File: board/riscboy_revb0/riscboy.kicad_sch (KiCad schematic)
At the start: 110 parts

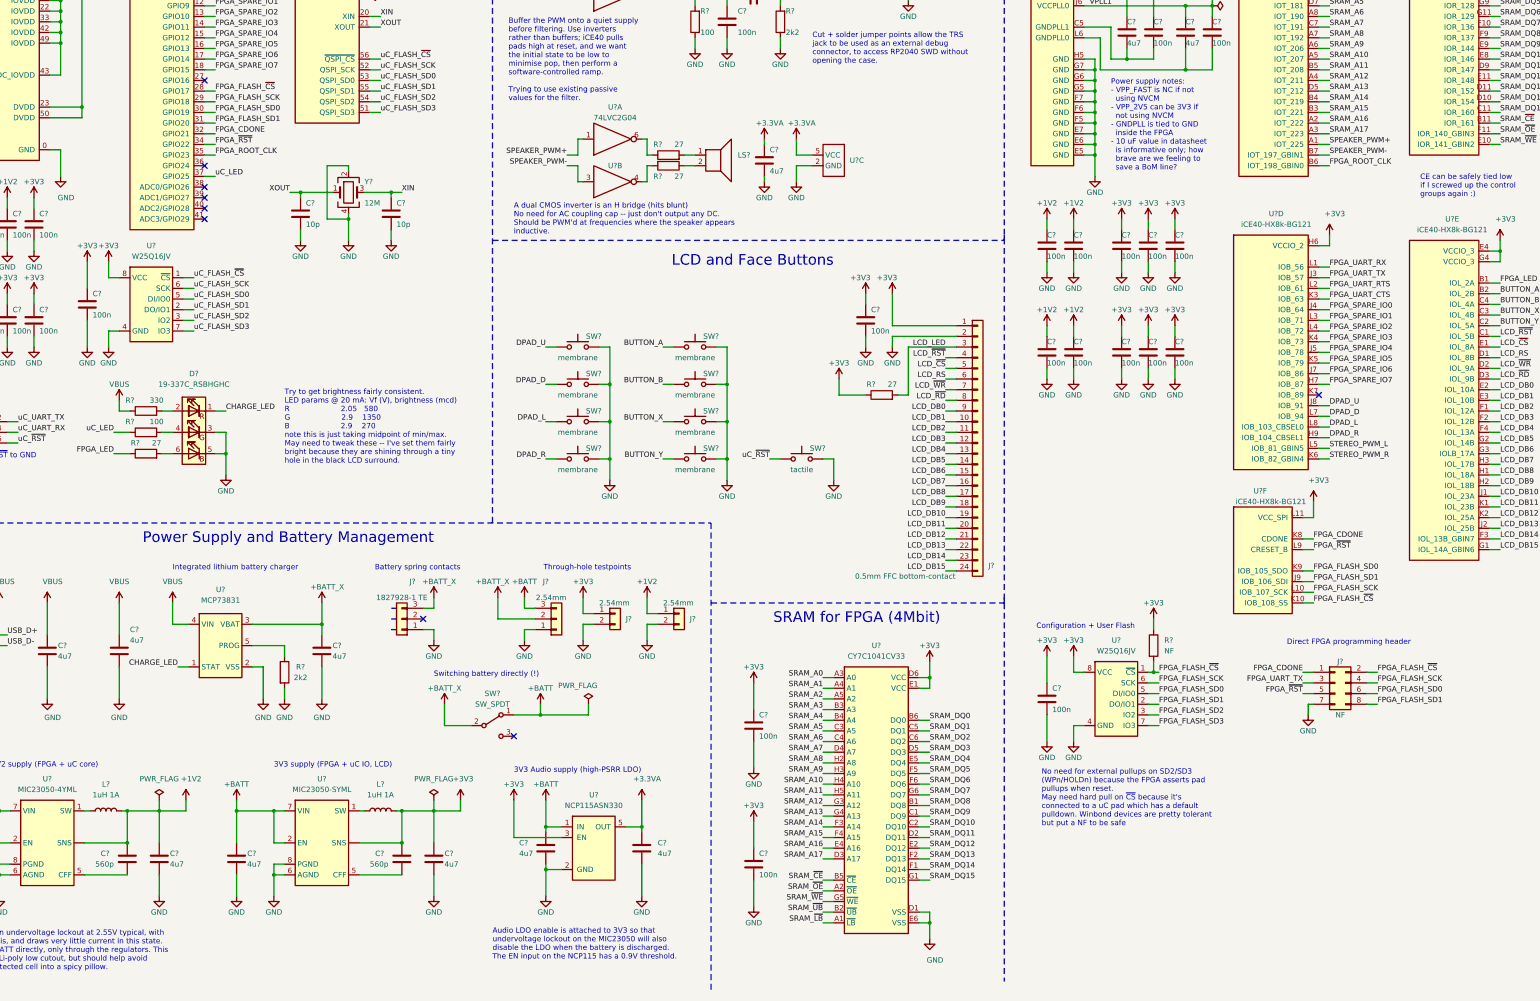
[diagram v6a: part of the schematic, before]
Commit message: Fix a couple of pin assignment issues found during review. Add 3V3A testpoint.
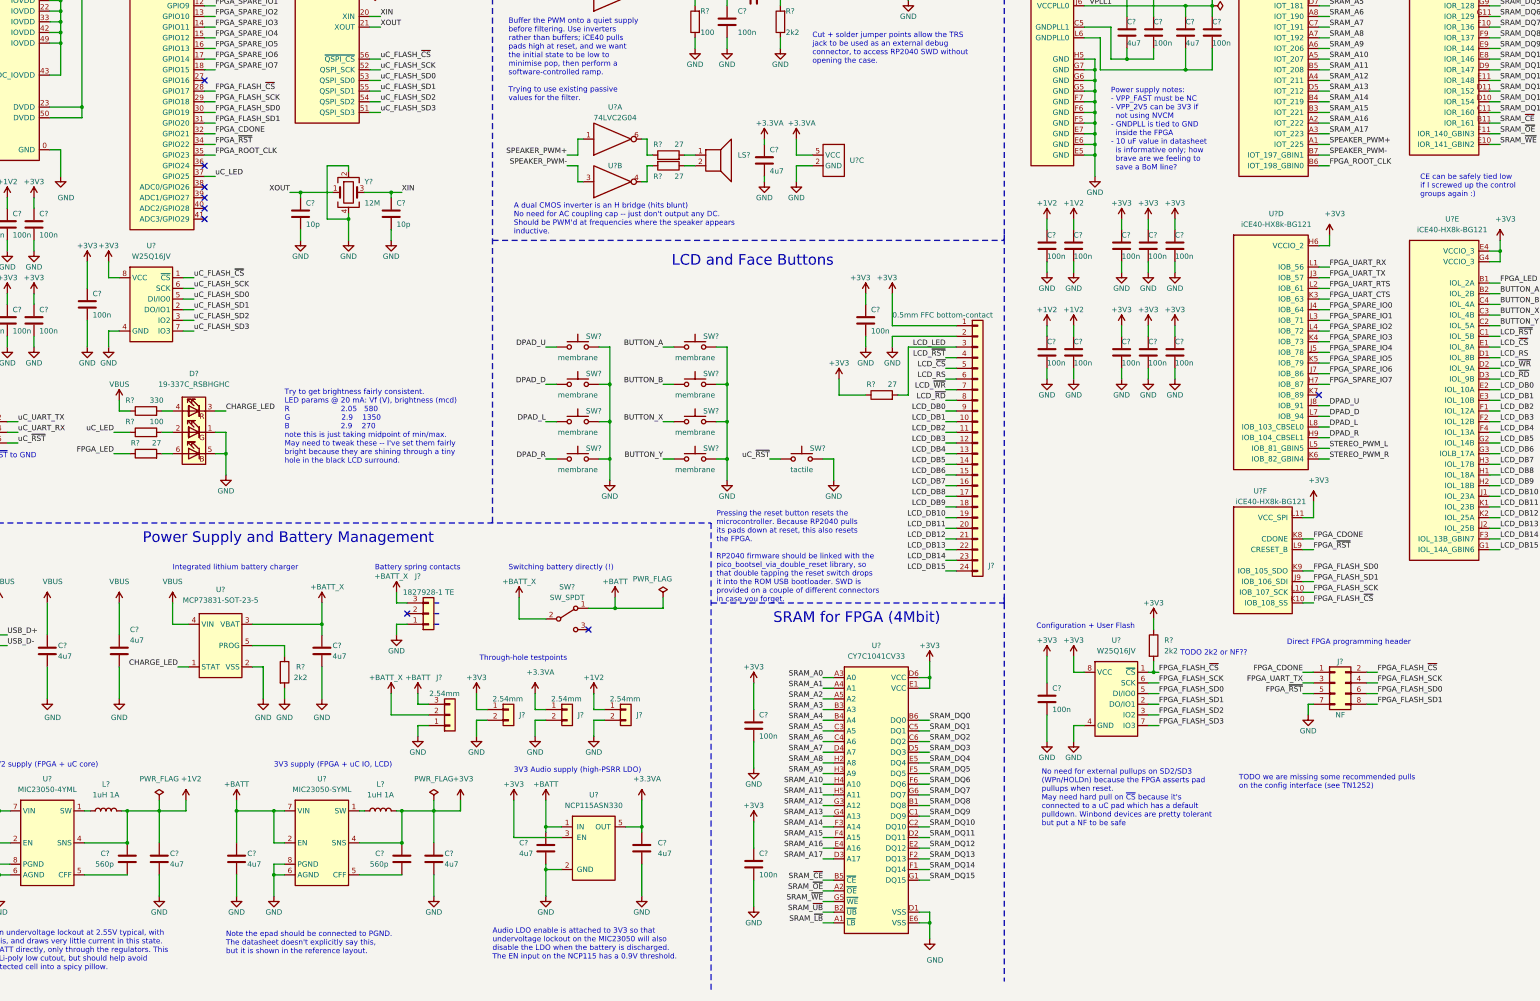
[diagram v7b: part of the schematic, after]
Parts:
- added J?: 2.54mm, symbol Connector_Generic:Conn_01x02
- R?: value NF -> 2k2
- U?: value MCP73831 -> MCP73831-SOT-23-5
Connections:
- net +1V2: now also U?.4 (SNS); no longer U?. (SNS)
- net +3.3VA: now also J?.1 (Pin_1)
- net +3V3: now also U?.4 (SNS); no longer U?. (SNS)
- net CHARGE_LED: now also D?.3 (GK); no longer D?.1 (RK)
- net GND: now also D?.1 (RK), J?.2 (Pin_2); no longer D?.3 (GK)
- net at R?.2: now also D?.4 (GA); no longer D?.2 (RA)
- net at R?.2: now also D?.2 (RA); no longer D?.4 (GA)
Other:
- note added: "Note the epad should be connected to PGND. The datasheet doesn't explicitly say this, but it is shown in the reference layout."
- note added: "Power supply notes: - VPP_FAST must be NC - VPP_2V5 can be 3V3 if not using NVCM - GNDPLL is tied to GND inside the FPGA - 10 uF value in datasheet is informative only; how brave are we feeling to save a BoM line?"
- note added: "Pressing the reset button resets the microcontroller. Because RP2040 pulls its pads down at reset, this also resets the FPGA. RP2040 firmware should be linked with the pico_bootsel_via_double_reset library, so that double tapping the reset switch drops it into the ROM USB bootloader. SWD is provided on a couple of different connectors in case you forget."
- note added: "TODO 2k2 or NF??"
- note added: "TODO we are missing some recommended pulls on the config interface (see TN1252)"
- note removed: "Power supply notes: - VPP_FAST is NC if not using NVCM - VPP_2V5 can be 3V3 if not using NVCM - GNDPLL is tied to GND inside the FPGA - 10 uF value in datasheet is informative only; how brave are we feeling to save a BoM line?"
- moved on the sheet: J?, SW?

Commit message: Finish first round of schematic review. Add a couple pullups, choose a power inductor :)
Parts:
- removed R?: 2k2, symbol Device:R
- added R13: NF, symbol Device:R
- added R17, R19, R20, R22: 2k2, symbol Device:R
- L1, L2: renamed from L?; value 1uH 1A -> BDCD002016101R0MS1
- gave numbers to parts that had none: 97
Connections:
- net +3V3: now also R13.1, R17.1, R19.1, R20.1, R22.1
- net FPGA_CDONE: now also R17.2
- net FPGA_FLASH_SCK: now also R20.2
- net FPGA_FLASH_~CS~: now also R22.2
- net FPGA_~RST~: now also R19.2
- net uC_~RST~: now also R13.2
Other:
- note added: "2k2 -> ~~450 mA charge current"
- note added: "All 4u7 caps are CL10A475KP8NNNC. This is a 10V-rated X5R cap. Note that 6.3V X5R caps lose *60%* of their capacitance at just 3.3V bias."
- note added: "I'm not convinced that all of these pullups are necessary, but they are all recommended by Lattice. Some of them can probably be marked no-fit for the next board revision, especially SCK which will drain a lot of current."
- note added: "No need for external pullups on SD2/SD3 (WPn/HOLDn) because the FPGA asserts pad pullups when reset."
- note added: "Reset is pulled up internally on RP2040, but add footprint for stronger pull. RP2040 firmware should be linked with the pico_bootsel_via_double_reset library, so that double tapping the reset switch drops it into the ROM USB bootloader. SWD is provided on a couple of different connectors in case you forget."
- note removed: "No need for external pullups on SD2/SD3 (WPn/HOLDn) because the FPGA asserts pad pullups when reset. May need hard pull on ~CS~ because it's connected to a uC pad which has a default pulldown. Winbond devices are pretty tolerant but put a NF to be safe"
- note removed: "Pressing the reset button resets the microcontroller. Because RP2040 pulls its pads down at reset, this also resets the FPGA. RP2040 firmware should be linked with the pico_bootsel_via_double_reset library, so that double tapping the reset switch drops it into the ROM USB bootloader. SWD is provided on a couple of different connectors in case you forget."
- note removed: "TODO 2k2 or NF??"
- note removed: "TODO we are missing some recommended pulls on the config interface (see TN1252)"
- moved on the sheet: C1, C11, C12, C44, J10, J4, J5, J6, J7, L1, SW1, SW10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
